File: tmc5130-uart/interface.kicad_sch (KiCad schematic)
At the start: 18 parts, among them J301 Molex_Pico-SPOX_Horizontal, J302 Molex_Pico-Lock-PLUS_Vertical, M301 Fan_5VDC_25x25x8mm, Q301 MOSFET-N-CH, U301 Switching_5V_500mA, U302 Linear_3.3V_1A

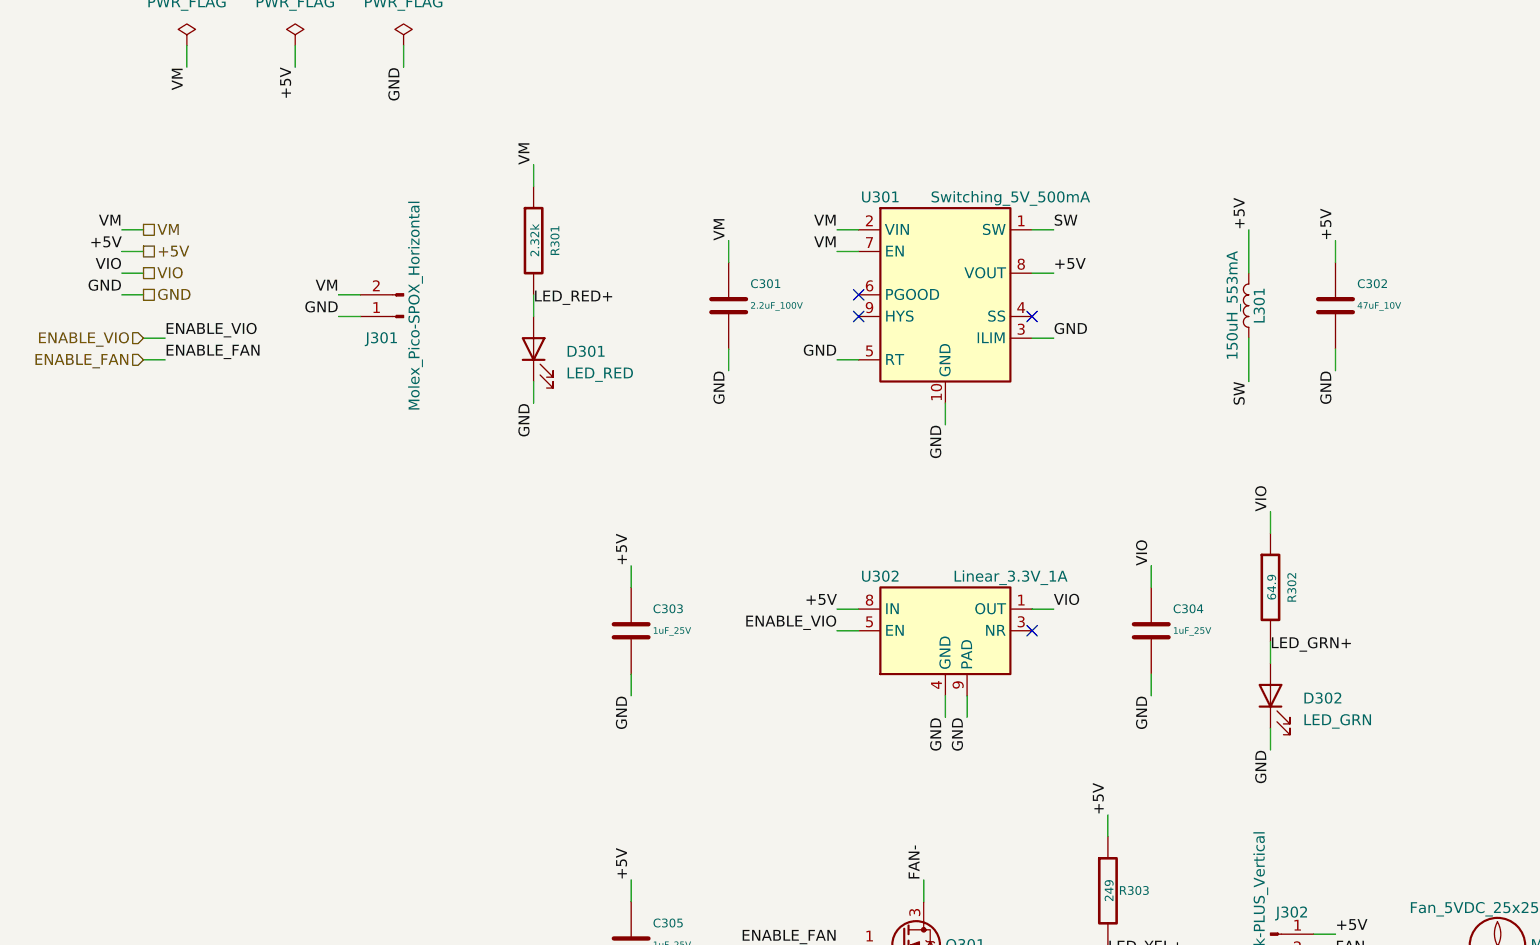
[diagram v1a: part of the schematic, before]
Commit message: TMC5160 -> TMC5130 component
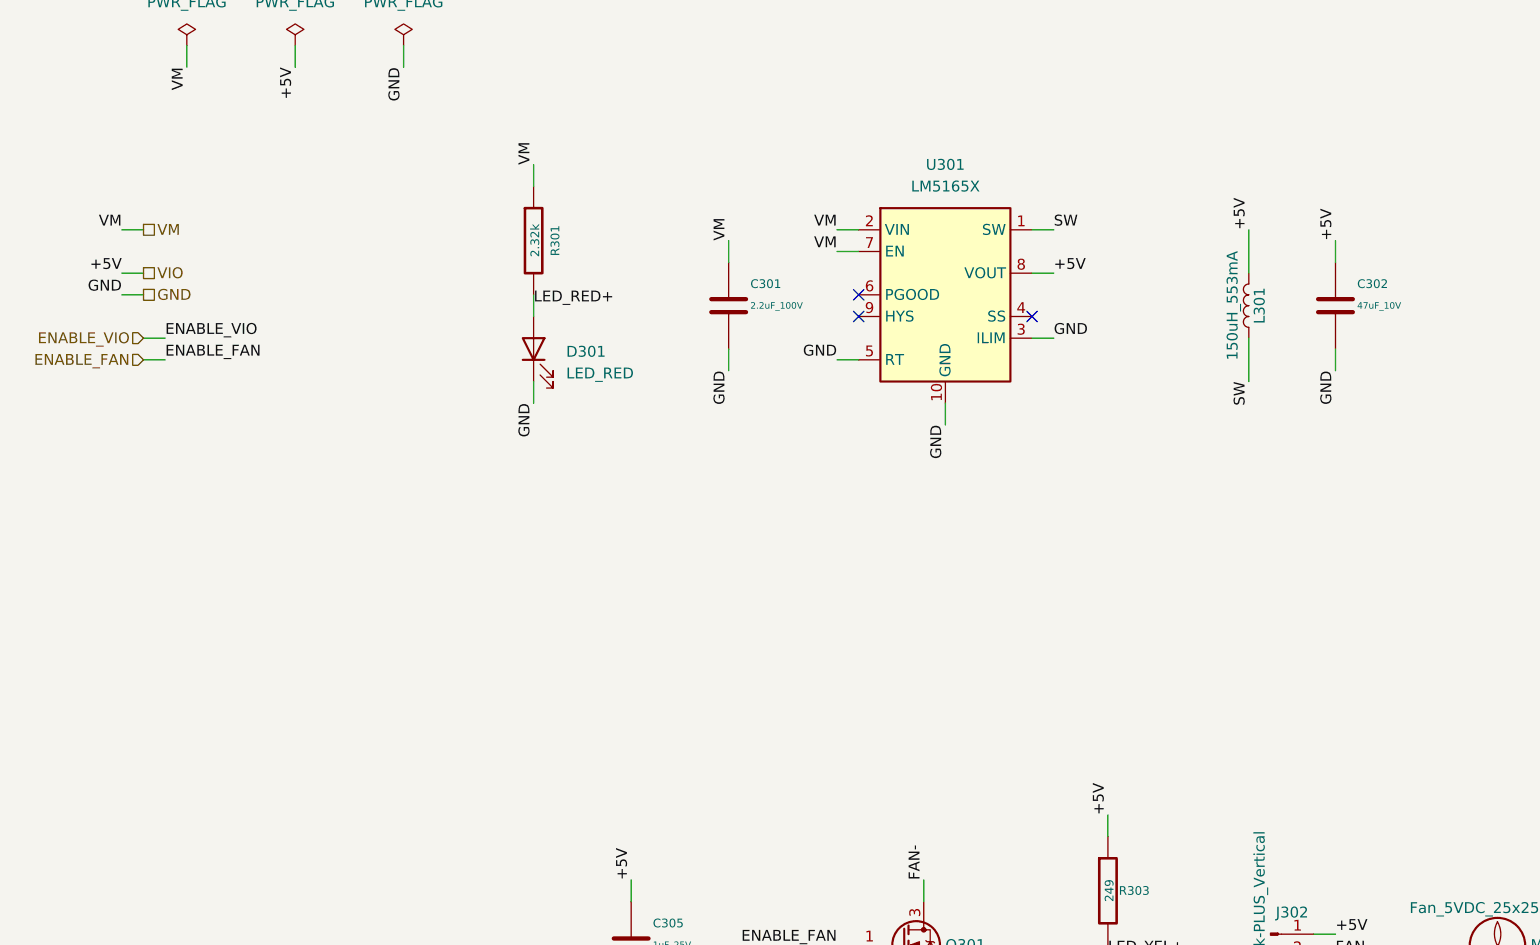
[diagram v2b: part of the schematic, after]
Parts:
- removed C303, C304: 1uF_25V, Janelia:C_0402_1005Metric, symbol Janelia:C_1uF_25V_0402
- removed D302: LED_GRN, Janelia:LED_0402-1005_KNB, symbol Janelia:LED_KNB_20mA_GRN_2.1V_0402
- removed J301: Molex_Pico-SPOX_Horizontal, Janelia:Molex_Pico-SPOX-87438_1x02-P1.5mm_Horizontal, symbol Janelia:Conn_01x02_P1.5mm_Molex_Pico-SPOX-87438_Horizontal
- removed R302: 64.9, Janelia:R_0402_1005Metric, symbol Janelia:R_64.9_0.1W_0402
- removed U301: Switching_5V_500mA, Janelia:Texas_S-PVSON-N10_ThermalVias, symbol Janelia:Regulator_Switching_5V_500mA_LM5166X
- removed U302: Linear_3.3V_1A, Janelia:TPS737Q1, symbol Janelia:Regulator_Linear_3.3V_1A_5.5Vin_TPS73733QDRBRQ1
- added U301: LM5165X, Package_SON:Texas_S-PVSON-N10_ThermalVias, symbol Janelia:LM5165X
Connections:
- net +5V is gone; now on net VIO: C302.1, C305.1, J302.1 (Pin_1), L301.2, R303.1
- net GND: now also U301.10 (GND), U301.11 (GND), U301.3 (ILIM), U301.5 (RT)
- net SW: now also U301.1 (SW)
- net VIO: now also U301.8 (VOUT)
- net VM: now also U301.2 (VIN), U301.7 (EN)
- no-connect marks 4 -> 3

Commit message: Add some components
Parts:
- added D302: D_Zener_47V_1W, Janelia:D_SMA, symbol Janelia:D_Zener_47V_1W
- added D304: D, symbol Janelia:D_1.25V@2A_400V
- added J301: FFC_P1mm_BOT_RA_SMD, symbol Janelia:Conn_01x10_FFC_P1mm_BOT_RA_SMD
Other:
- moved on the sheet: C301, C302, C305, D301, D303, J302, L301, M301, Q301, R301, R303, U301

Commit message: Add components
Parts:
- added R302: 0.24, Janelia:R_2512_6332Metric, symbol Janelia:R_0.240_1W_2512
- J301: footprint (none) -> Janelia:CONN_C2914097; Vendor (none) -> JLCPCB; Vendor Part Number (none) -> C2914097
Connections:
- net GND: now also D302.2 (A), J301.3 (Pin_3), J301.4 (Pin_4), J301.5 (Pin_5), J301.6 (Pin_6)
- net VBB: now reaches D302.1 (K)
- net VBB: now also D304.2 (A), R302.2
- net VCC: now reaches D304.1 (K)
- net SWN: now reaches J301.1 (Pin_1)
- net VAA: now reaches J301.10 (Pin_10)
- net VAA: now also J301.7 (Pin_7), J301.8 (Pin_8), J301.9 (Pin_9), R302.1
- net SWP: now reaches J301.2 (Pin_2)
- net VIO renamed +5V
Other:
- moved on the sheet: C305, D302, D304, J301, M301

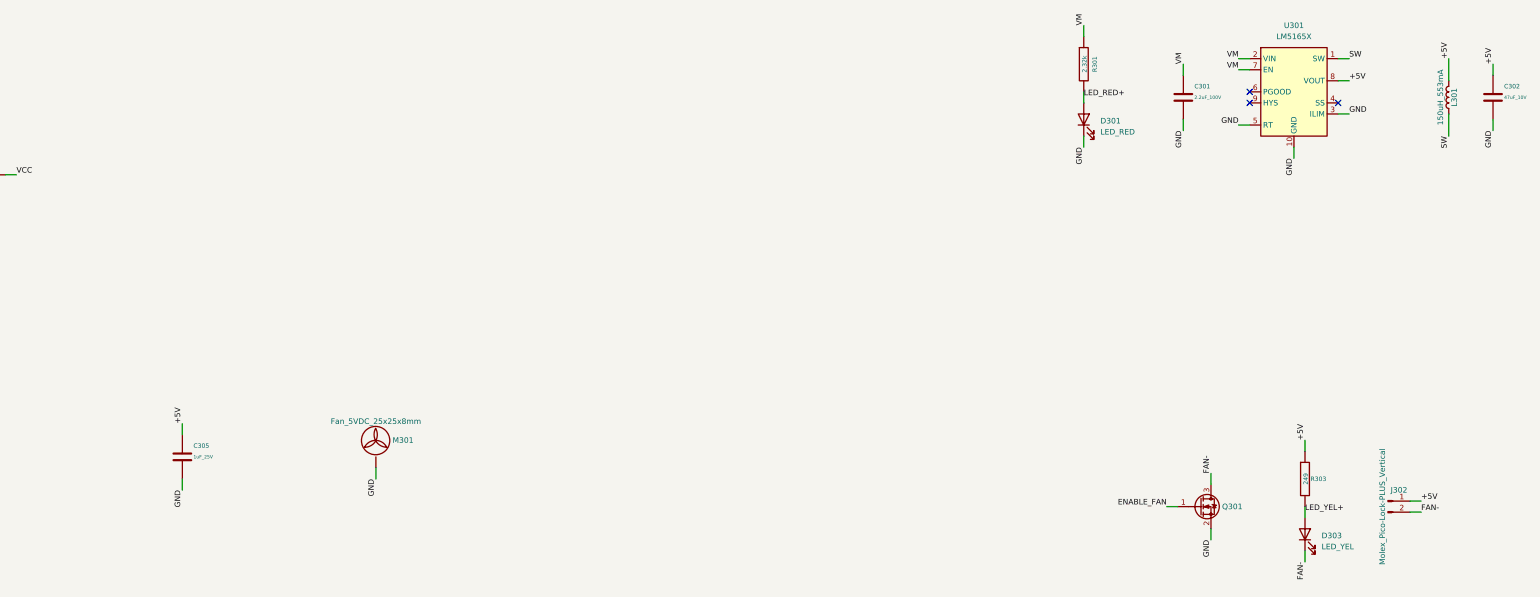
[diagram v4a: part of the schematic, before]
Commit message: Add components from jlcpcb
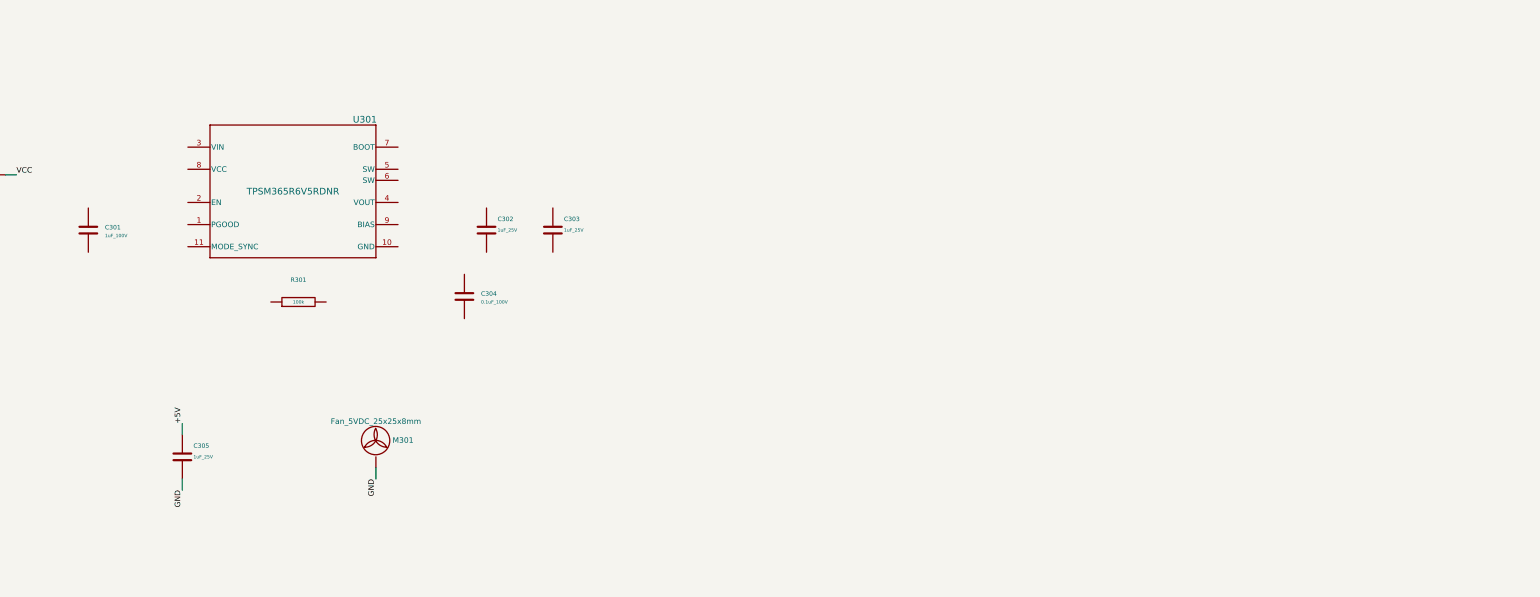
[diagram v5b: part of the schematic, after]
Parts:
- removed C301: 2.2uF_100V, Janelia:C_0805_2012Metric, symbol Janelia:C_2.2uF_100V_0805
- removed C302: 47uF_10V, Janelia:C_0805_2012Metric, symbol Janelia:C_47uF_10V_0805
- removed D301: LED_RED, Janelia:LED_0402-1005_KNB, symbol Janelia:LED_KNB_20mA_RED_1.95V_0402
- removed D303: LED_YEL, Janelia:LED_0402-1005_KNB, symbol Janelia:LED_KNB_20mA_YEL_2V_0402
- removed J302: Molex_Pico-Lock-PLUS_Vertical, Janelia:Molex_Micro-Lock-PLUS-505568_1x02_P1.25mm_Vertical, symbol Janelia:Conn_01x02_P1.25mm_Molex_Micro-Lock-PLUS-505568_Vertical
- removed L301: 150uH_553mA, Janelia:IND_CB_SD25, symbol Janelia:L_150uH_553mA
- removed Q301: MOSFET-N-CH, Janelia:XFDFN-3, symbol Janelia:MOSFET-N-CH-EN-CSD17483F4
- removed R301: 2.32k, Janelia:R_0805_2012Metric, symbol Janelia:R_2.32k_1W_0805
- removed R303: 249, Janelia:R_0402_1005Metric, symbol Janelia:R_249_0.06W_0402
- removed U301: LM5165X, Package_SON:Texas_S-PVSON-N10_ThermalVias, symbol Janelia:LM5165X
- added C301: 1uF_100V, Janelia:C_0805_2012Metric, symbol Janelia:C_1uF_100V_0805
- added C302, C303: 1uF_25V, Janelia:C_0402_1005Metric, symbol Janelia:C_1uF_25V_0402
- added C304: 0.1uF_100V, Janelia:C_0402_1005Metric, symbol Janelia:C_0.1uF_100V_0402
- added R301: 100k, Janelia:R_0402_1005Metric, symbol Janelia:R_100k_0402
- added U301: TPSM365R6V5RDNR, Janelia:RDN0011A-MFG, symbol Janelia:TPSM365R6V5RDNR
- D304: footprint (none) -> Janelia:D_SMB
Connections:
- no-connect marks 3 -> 0

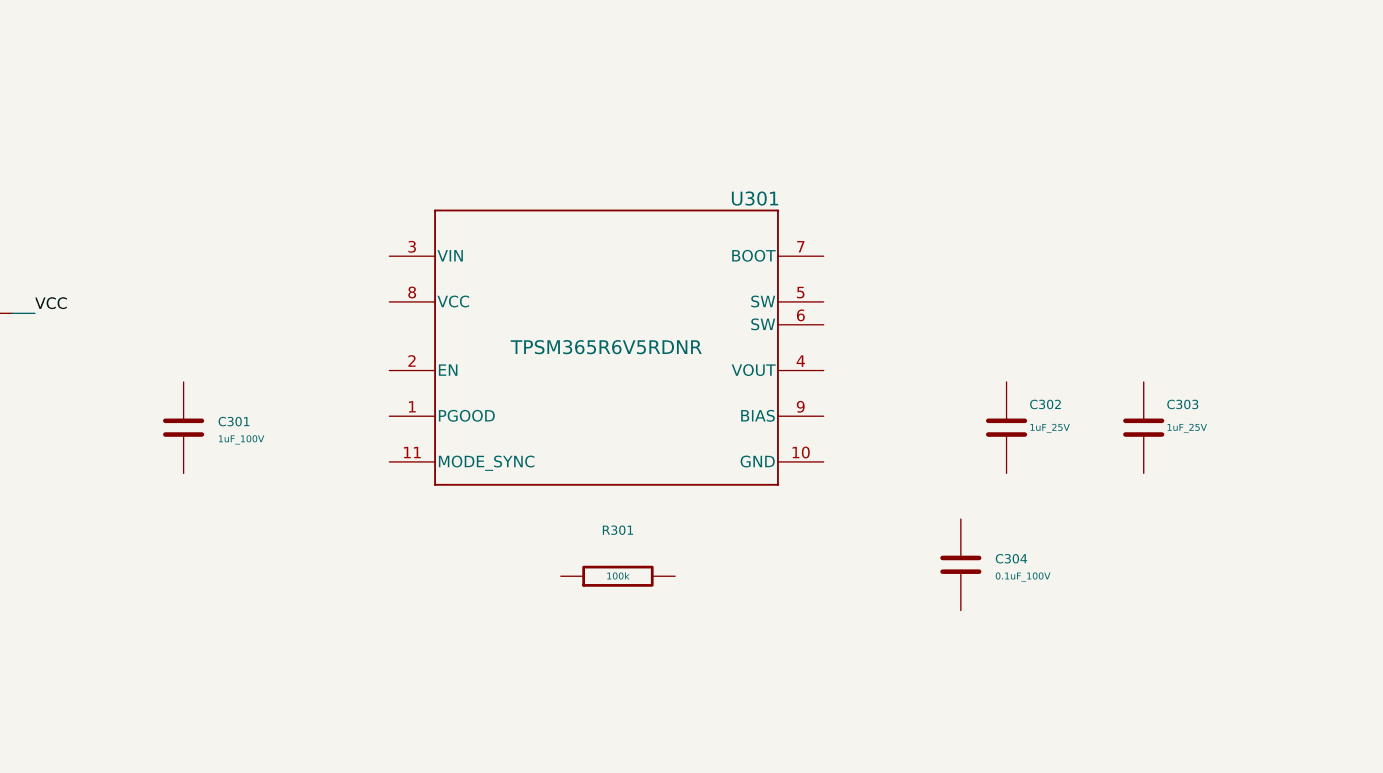
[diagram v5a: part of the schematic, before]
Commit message: Connect DC/DC
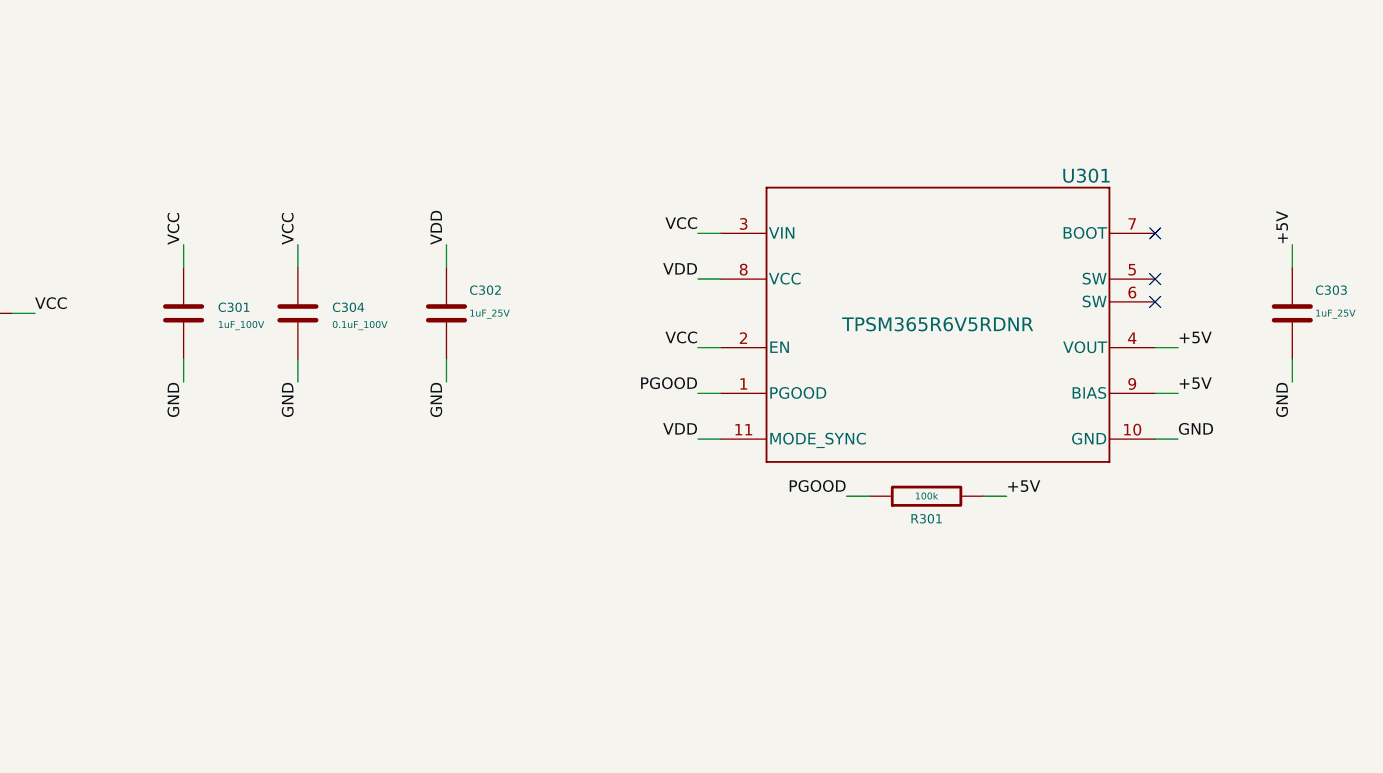
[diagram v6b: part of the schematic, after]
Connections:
- net +5V: now also C303.1, R301.2, U301.4 (VOUT), U301.9 (BIAS)
- net GND: now also C301.2, C302.2, C303.2, C304.2, U301.10 (GND)
- net VCC: now also C301.1, C304.1, U301.2 (EN), U301.3 (VIN)
- net PGOOD: now reaches R301.1
- net PGOOD: now also U301.1 (PGOOD)
- net VDD: now reaches U301.11 (MODE_SYNC)
- net VDD: now also C302.1, U301.8 (VCC)
- no-connect marks 0 -> 3
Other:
- moved on the sheet: C301, C302, C303, C304, R301, U301

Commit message: Switch capacitor
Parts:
- removed C301: 1uF_100V, Janelia:C_0805_2012Metric, symbol Janelia:C_1uF_100V_0805
- added C301: 1uF_100V, Janelia:C_1206_3216Metric, symbol Janelia:C_1uF_100V_1206
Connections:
- net GND: now also C301.2
- net VCC: now also C301.1
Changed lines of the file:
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@@
+    )
+  )
+  (symbol (lib_id "Janelia:C_1uF_100V_1206") (at 132.08 68.58 0) (unit 1)
+    (in_bom yes) (on_board yes) (dnp no) (fields_autoplaced)
+    (property "Reference" "C301" (at 135.89 67.945 0)
+      (effects (font (size 1.016 1.016)) (justify left))
+    )
+    (property "Value" "1uF_100V" (at 135.89 69.8499 0)
+      (effects (font (size 0.762 0.762)) (justify left))
+    )
+    (property "Footprint" "Janelia:C_1206_3216Metric" (at 133.0452 72.39 0)
+      (effects (font (size 0.762 0.762)) hide)
+    )
+    (property "Datasheet" "" (at 132.08 68.58 0)
+      (effects (font (size 1.524 1.524)) hide)
+    )
+    (property "Vendor" "JLCPCB" (at 134.62 63.5 0)
+      (effects (font (size 1.524 1.524)) hide)
+    )
+    (property "Vendor Part Number" "C840122" (at 137.16 60.96 0)
+      (effects (font (size 1.524 1.524)) hide)
+    )
+    (property "Synopsis" "100V 1uF X7R ±20% 1206" (at 139.7 58.42 0)
+      (effects (font (size 1.524 1.524)) hide)
+    )
+    (property "Package" "1206" (at 132.08 68.58 0)
+      (effects (font (size 1.27 1.27)) hide)
+    )
+    (property "Manufacturer" "HUI JU" (at 132.08 68.58 0)
+      (effects (font (size 1.27 1.27)) hide)
+    )
+    (property "Manufacturer Part Number" "NC1206B105M101CEPN" (at 132.08 68.58 0)
+      (effects (font (size 1.27 1.27)) hide)
+    )
+    (property "LCSC" "C840122" (at 132.08 68.58 0)
+      (effects (font (size 1.27 1.27)) hide)
+    )
+    (pin "1")
+    (pin "2")
+    (instances
+      (project "tmc5130-uart"
+        (path "/df2b2e89-e055-4140-95de-f1df723db034/c1dd8f61-494c-402f-8e59-08309c64fc3f"
+          (reference "C301") (unit 1)
+        )
+      )
     )
   )
@@
         )
       )
-    )
-  )
-  (symbol (lib_id "Janelia:C_1uF_100V_0805") (at 132.08 68.58 0) (unit 1)
-    (in_bom yes) (on_board yes) (dnp no) (fields_autoplaced)
-    (property "Reference" "C301" (at 135.89 67.945 0)
-      (effects (font (size 1.016 1.016)) (justify left))
-    )
-    (property "Value" "1uF_100V" (at 135.89 69.8499 0)
-      (effects (font (size 0.762 0.762)) (justify left))
-    )
-    (property "Footprint" "Janelia:C_0805_2012Metric" (at 133.0452 72.39 0)
-      (effects (font (size 0.762 0.762)) hide)
-    )
-    (property "Datasheet" "" (at 132.08 68.58 0)
-      (effects (font (size 1.524 1.524)) hide)
-    )
-    (property "Vendor" "JLCPCB" (at 134.62 63.5 0)
-      (effects (font (size 1.524 1.524)) hide)
-    )
-    (property "Vendor Part Number" "C559300" (at 137.16 60.96 0)
-      (effects (font (size 1.524 1.524)) hide)
-    )
-    (property "Synopsis" "CAP CER 1UF 100V X7R" (at 139.7 58.42 0)
-      (effects (font (size 1.524 1.524)) hide)
-    )
-    (property "Package" "0805" (at 132.08 68.58 0)
-      (effects (font (size 1.27 1.27)) hide)
-    )
-    (property "Manufacturer" "IHHEC" (at 132.08 68.58 0)
-      (effects (font (size 1.27 1.27)) hide)
-    )
-    (property "Manufacturer Part Number" "C0805X105K101TDXF" (at 132.08 68.58 0)
-      (effects (font (size 1.27 1.27)) hide)
-    )
-    (property "LCSC" "C559300" (at 132.08 68.58 0)
-      (effects (font (size 1.27 1.27)) hide)
-    )
-    (pin "2")
-    (pin "1")
-    (instances
-      (project "tmc5130-uart"
-        (path "/df2b2e89-e055-4140-95de-f1df723db034/c1dd8f61-494c-402f-8e59-08309c64fc3f"
-          (reference "C301") (unit 1)
-        )
-      )
